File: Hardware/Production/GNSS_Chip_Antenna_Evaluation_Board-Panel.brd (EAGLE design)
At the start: 61 x 35.6 mm, 70 parts, among them J1 U.FL, J2 U.FL, J3 U.FL, J4 U.FL, J5 U.FL, J6 U.FL, Y2 PUCK, Y3 CUBE, Y4 CHIP, Y5 MOLDED, Y6 W3062A, Y7 W3011

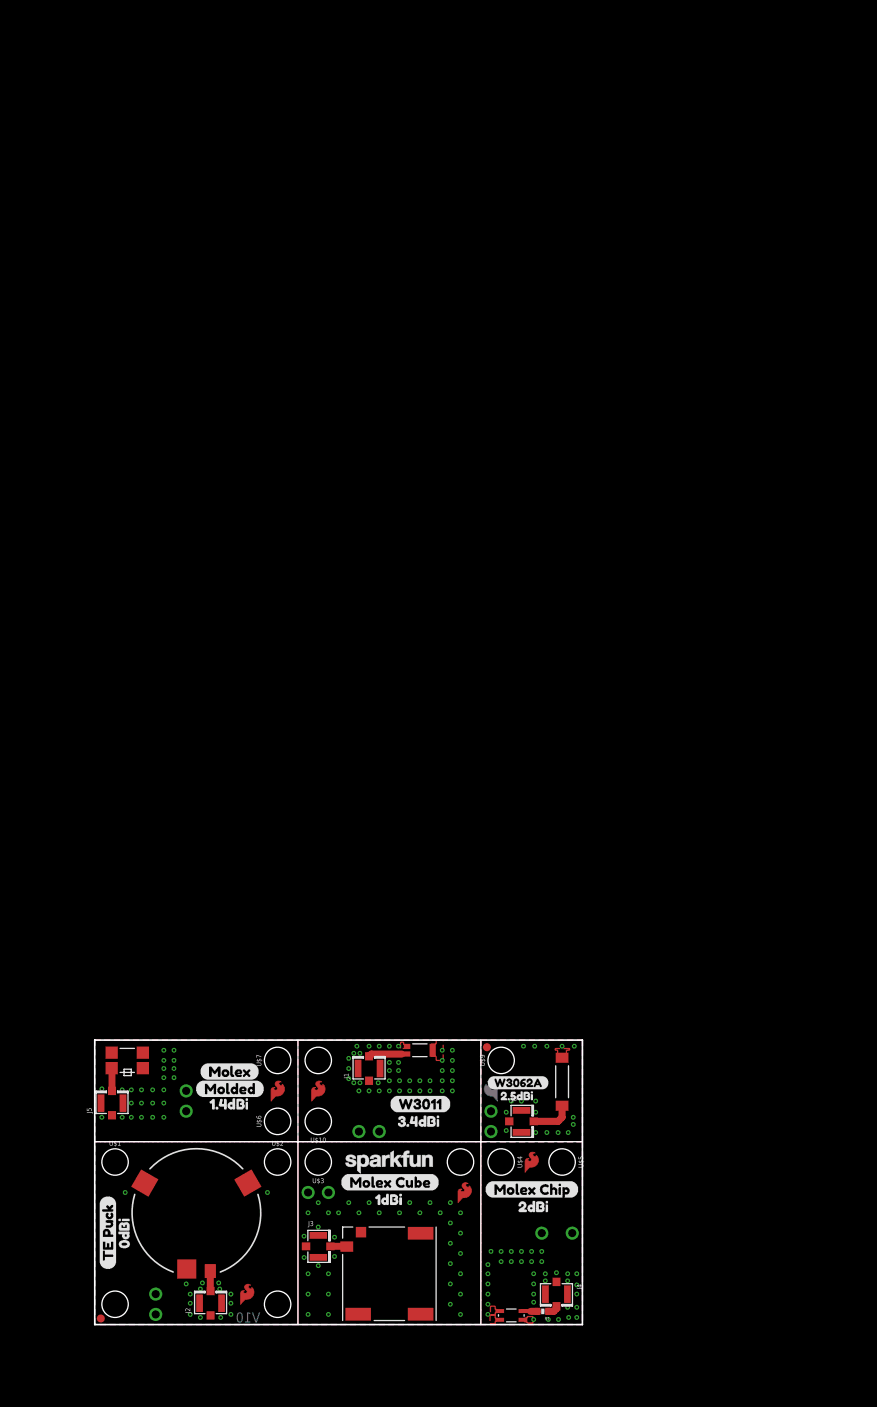
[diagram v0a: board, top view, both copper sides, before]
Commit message: Adding production panel
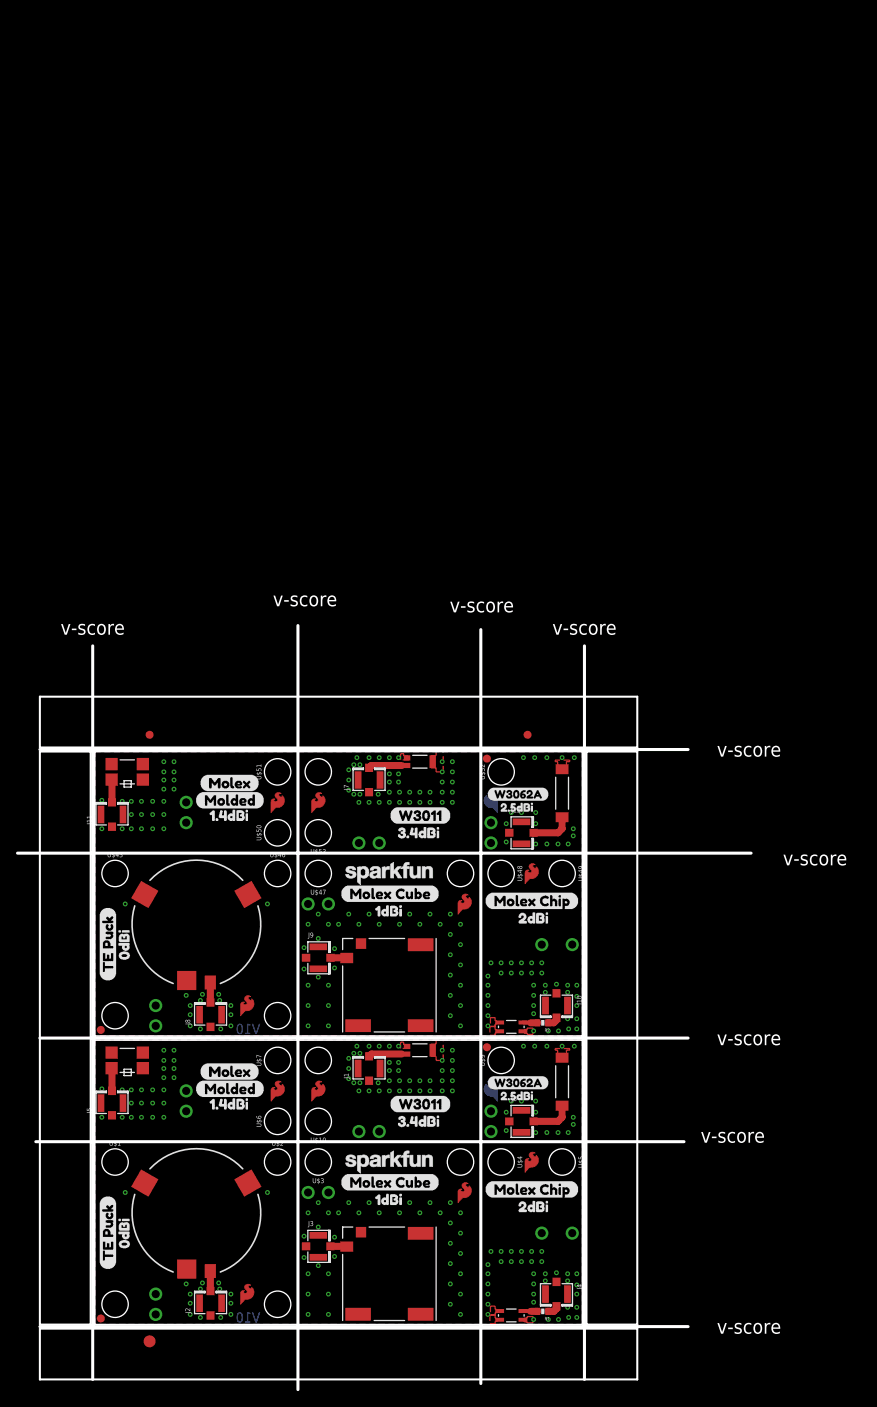
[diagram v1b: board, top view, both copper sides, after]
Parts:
- removed FRAME1: FRAME-LETTER, SparkFun-Aesthetics:CREATIVE_COMMONS
- added E$1, E$2: (no value), SparkFun-Aesthetics:FIDUCIAL-1X2
- added E$3: (no value), SparkFun-Retired:FIDUCIAL-1.5X3
- added J10, J11, J12, J7, J8, J9: U.FL, SparkFun-Connectors:U.FL
- added JP10, JP7: FIDUCIAL1X2, SparkFun:FIDUCIAL-1X2
- added JP11, JP12, JP3, JP4: STAND-OFF, SparkFun:STAND-OFF
- added LOGO10, LOGO11, LOGO12, LOGO7, LOGO8, LOGO9: SFE_LOGO_FLAME.1EXP, SparkFun-Aesthetics:SFE_LOGO_FLAME_COPPER_EXPOSED_.1
- added R2: 0, Testing:0402-RES
- added U$43, U$46, U$47, U$48, U$49, U$50, U$51, U$52, U$53: (no value), SparkFun-Hardware:STAND-OFF
- added U$54, U$75: (no value), buzzard_labels (13):3#4DBI2
- added U$55, U$74: (no value), buzzard_labels (13):W30111
- added U$56, U$83: (no value), buzzard_labels (14):0DBI0
- added U$57, U$73: (no value), buzzard_labels (14):1#4DBI3
- added U$58, U$80: (no value), buzzard_labels (14):1DBI1
- added U$59, U$79: (no value), buzzard_labels (14):2DBI2
- added U$60, U$78: (no value), buzzard_labels (14):MOLEX_CHIP7
- added U$61, U$81: (no value), buzzard_labels (14):MOLEX_CUBE6
- added U$62, U$82: (no value), buzzard_labels (14):TE_PUCK5
- added U$63, U$64, U$65, U$66, U$67, U$68: (no value), buzzard_labels (60):ANCHOR0
- added U$69, U$72: (no value), buzzard_labels (60):MOLDED2
- added U$70, U$71: (no value), buzzard_labels (60):MOLEX1
- added U$76: (no value), buzzard_labels (14):W3062A9
- added U$77: (no value), buzzard_labels (14):2#5DBI4
- added U$84: (no value), buzzard_labels (61):2#5DBI2
- added U$85: (no value), buzzard_labels (61):W3062A1
- added U$86: (no value), SparkFun-Aesthetics:SFE_LOGO_NAME_.1
- added Y1: PUCK, GNSS_Chip_Antenna_Evaluation_Board:TE_PUCK
- added Y10: MOLDED, GNSS_Chip_Antenna_Evaluation_Board:MLOEX_GNSS_MOLDED
- added Y11: W3062A, GNSS_Chip_Antenna_Evaluation_Board:W3062A
- added Y12: W3011, GNSS_Chip_Antenna_Evaluation_Board:W3011
- added Y8: CUBE, GNSS_Chip_Antenna_Evaluation_Board:MOLEX_GNSS_CUBE
- added Y9: CHIP, GNSS_Chip_Antenna_Evaluation_Board:MOLEX_GNSS_CHIP
- U$17: value (none) -> OSHW-LOGOS; device SparkFun-Aesthetics:ORDERING_INSTRUCTIONS -> SparkFun-Aesthetics:OSHW-LOGO-S
- moved U$17 47.0 mm to (19.1, 39.9), flipped to the bottom
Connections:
- new net FEED10: J10.FEED, R2.1
- new net FEED11: J11.FEED, Y10.FEED
- new net FEED12: J12.FEED, Y11.FEED
- new net FEED7: J7.FEED, Y12.1
- new net FEED8: J8.FEED, Y1.S
- new net FEED9: J9.FEED, Y8.FEED
- new net GND1: J10.1, J10.2, J11.1, J11.2, J12.1, J12.2, J7.1, J7.2, J8.1, J8.2, J9.1, J9.2, Y1.1, Y1.2, Y1.3, Y11.GND, Y12.2, Y12.3, Y8.GND, Y9.1, Y9.2, Y9.3
- new net N$2: R2.2, Y9.FEED
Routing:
- net FEED12: track 0.00 -> 5.21 mm
- net FEED7: track 0.00 -> 5.12 mm
- net FEED11: track 0.00 -> 2.92 mm
- net FEED8: track 0.00 -> 2.51 mm
- net FEED9: track 0.00 -> 2.09 mm
- net N$2: track 0.00 -> 1.86 mm
- net FEED10: track 0.00 -> 1.50 mm
- added copper zone on layer 1, net GND1
- added copper zone on layer 16, net GND1
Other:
- board size 61 x 35.6 mm -> 91.7 x 95.5 mm
- board text added: "v-score"
- board text removed: "0.8mm Board Thickness"
- board text removed: "D:/SmartProjects/Snc/a4_bn_logo2.bmp"

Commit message: Corrected the polygon FP issue on the U.FL.
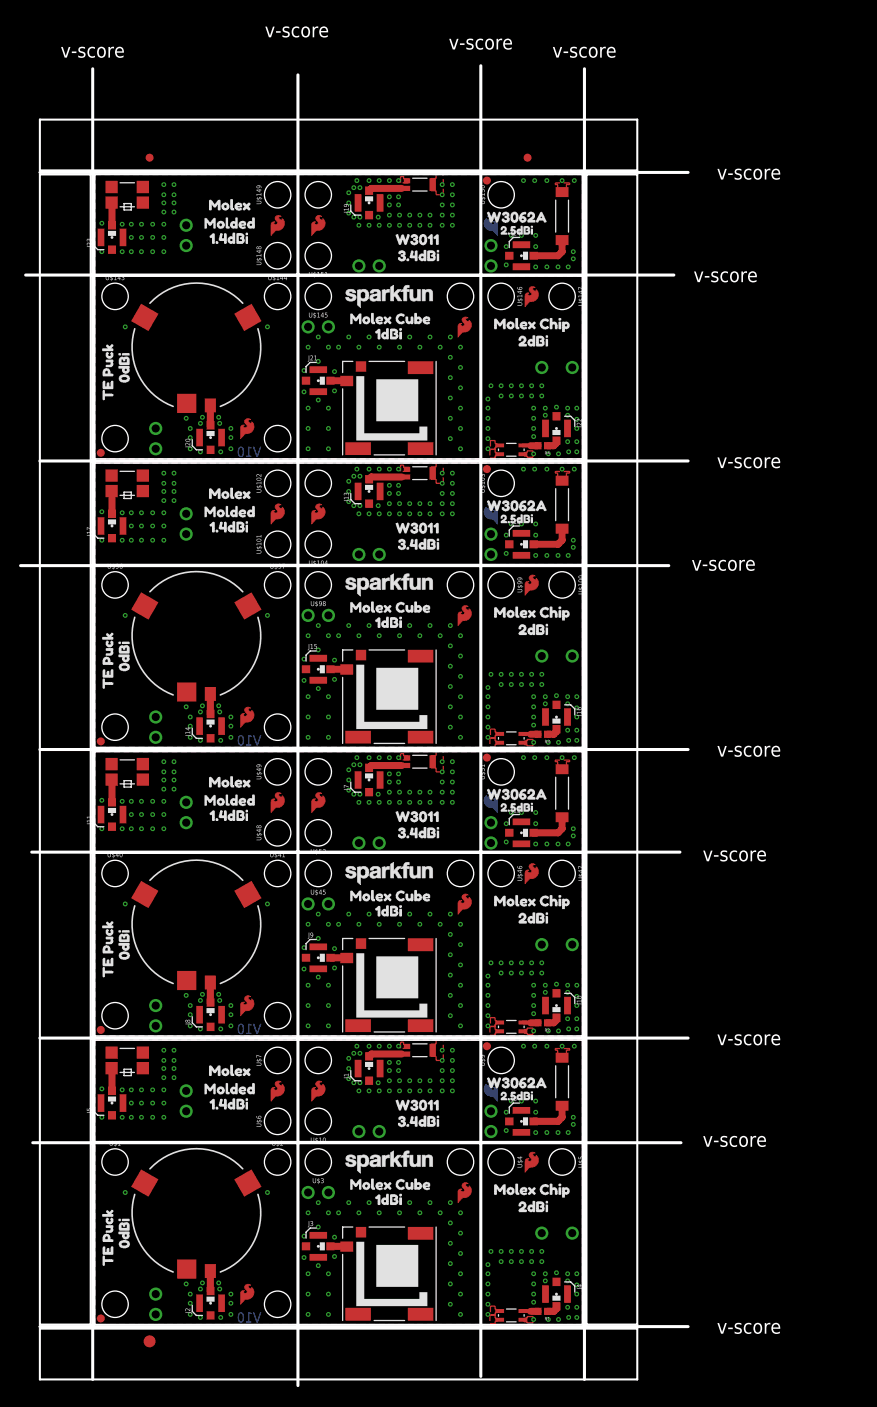
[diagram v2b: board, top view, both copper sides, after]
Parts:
- added J13, J14, J15, J16, J17, J18, J19, J20, J21, J22, J23, J24: U.FL, SparkFun-Connectors:U.FL
- added JP13, JP14, JP17, JP18, JP19, JP20, JP23, JP24: STAND-OFF, SparkFun:STAND-OFF
- added JP15, JP16, JP21, JP22: FIDUCIAL1X2, SparkFun:FIDUCIAL-1X2
- added LOGO13, LOGO14, LOGO15, LOGO16, LOGO17, LOGO18, LOGO19, LOGO20, LOGO21, LOGO22, LOGO23, LOGO24: SFE_LOGO_FLAME.1EXP, SparkFun-Aesthetics:SFE_LOGO_FLAME_COPPER_EXPOSED_.1
- added R3, R4: 0, SparkFun-Resistors:0402
- added U$100, U$101, U$102, U$103, U$104, U$143, U$144, U$145, U$146, U$147, U$148, U$149, U$150, U$151, U$96, U$97, U$98, U$99: (no value), SparkFun-Hardware:STAND-OFF
- added U$105, U$117, U$152, U$164: (no value), buzzard_labels (13):3#4DBI2
- added U$106, U$121, U$153, U$168: (no value), buzzard_labels (14):0DBI0
- added U$107, U$116, U$154, U$163: (no value), buzzard_labels (14):1#4DBI3
- added U$108, U$120, U$155, U$167: (no value), buzzard_labels (14):1DBI1
- added U$109, U$119, U$156, U$166: (no value), buzzard_labels (14):2DBI2
- added U$110, U$111, U$112, U$113, U$114, U$115, U$157, U$158, U$159, U$160, U$161, U$162: (no value), buzzard_labels (60):ANCHOR0
- added U$118, U$165: (no value), buzzard_labels (14):2#5DBI4
- added U$122, U$169: (no value), buzzard_labels (61):2#5DBI2
- added U$123, U$170: (no value), SparkFun-Aesthetics:SFE_LOGO_NAME_.1
- added U$124, U$171: (no value), buzzard_labels (1):ANTENNA10
- added U$125, U$172: (no value), buzzard_labels (1):EVALUATION_BOARD15
- added U$126, U$173: (no value), buzzard_labels (1):GNSS_CHIP13
- added U$127, U$138, U$174, U$185, U$91: (no value), buzzard_labels (1):MOLEX_CUBE6
- added U$128, U$131, U$175, U$178: (no value), buzzard_labels (1):TE_PUCK7
- added U$129, U$140, U$176, U$187, U$93: (no value), buzzard_labels (1):W3062A3
- added U$130, U$139, U$177, U$186, U$92: (no value), buzzard_labels (1):W30112
- added U$132, U$133, U$179, U$180: (no value), buzzard_labels (1):MOLEX_CHIP5
- added U$134, U$136, U$181, U$183, U$87, U$89: (no value), buzzard_labels (1):MOLEX0
- added U$135, U$137, U$182, U$184, U$88, U$90: (no value), buzzard_labels (1):MOLDED1
- added U$141, U$188, U$94: (no value), SparkFun-Aesthetics:SFE_LOGO_NAME_FLAME_.1
- added U$142, U$95: OSHW-LOGOS, SparkFun-Aesthetics:OSHW-LOGO-S
- added Y13, Y19: PUCK, SparkFun-GPS:TE_PUCK
- added Y14, Y20: CUBE, SparkFun-GPS:MOLEX_GNSS_CUBE
- added Y15, Y21: CHIP, SparkFun-GPS:MOLEX_GNSS_CHIP
- added Y16, Y22: MOLDED, SparkFun-GPS:MLOEX_GNSS_MOLDED
- added Y17, Y23: W3062A, SparkFun-GPS:W3062A
- added Y18, Y24: W3011, SparkFun-GPS:W3011
- R1, R2: device Testing:0402-RES -> SparkFun-Resistors:0402
- U$13: device buzzard_labels (13):W30111 -> buzzard_labels (1):TE_PUCK7
- U$19: device buzzard_labels (14):MOLEX_CHIP7 -> buzzard_labels (1):MOLEX_CHIP5
- U$20: device buzzard_labels (14):MOLEX_CUBE6 -> buzzard_labels (1):MOLEX_CHIP5
- U$21: device buzzard_labels (60):MOLEX1 -> buzzard_labels (1):MOLEX0
- U$22: device buzzard_labels (14):TE_PUCK5 -> buzzard_labels (1):MOLEX0
- U$29: device buzzard_labels (60):MOLDED2 -> buzzard_labels (1):MOLDED1
- U$30: device buzzard_labels (60):MOLEX1 -> buzzard_labels (1):MOLDED1
- U$31: device buzzard_labels (60):MOLDED2 -> buzzard_labels (1):MOLEX_CUBE6
- U$33: device buzzard_labels (13):W30111 -> buzzard_labels (1):W30112
- U$35: device buzzard_labels (14):W3062A9 -> buzzard_labels (1):W3062A3
- U$37: device buzzard_labels (14):MOLEX_CHIP7 -> SparkFun-Aesthetics:SFE_LOGO_NAME_FLAME_.1
- U$40: device buzzard_labels (14):MOLEX_CUBE6 -> SparkFun-Hardware:STAND-OFF
- U$41: device buzzard_labels (14):TE_PUCK5 -> SparkFun-Hardware:STAND-OFF
- U$43: device SparkFun-Hardware:STAND-OFF -> buzzard_labels (1):ANTENNA10
- U$45: device buzzard_labels (61):W3062A1 -> SparkFun-Hardware:STAND-OFF
- U$50: device SparkFun-Hardware:STAND-OFF -> buzzard_labels (1):EVALUATION_BOARD15
- U$52: device SparkFun-Hardware:STAND-OFF -> buzzard_labels (1):GNSS_CHIP13
- U$55, U$74: device buzzard_labels (13):W30111 -> buzzard_labels (14):0DBI0
- U$56: device buzzard_labels (14):0DBI0 -> buzzard_labels (1):MOLEX_CUBE6
- U$57: device buzzard_labels (14):1#4DBI3 -> buzzard_labels (1):TE_PUCK7
- U$58: device buzzard_labels (14):1DBI1 -> buzzard_labels (1):W3062A3
- U$59: device buzzard_labels (14):2DBI2 -> buzzard_labels (1):W30112
- U$60: device buzzard_labels (14):MOLEX_CHIP7 -> buzzard_labels (14):1#4DBI3
- U$61: device buzzard_labels (14):MOLEX_CUBE6 -> buzzard_labels (14):1DBI1
- U$62: device buzzard_labels (14):TE_PUCK5 -> buzzard_labels (14):2DBI2
- U$69: device buzzard_labels (60):MOLDED2 -> buzzard_labels (14):1#4DBI3
- U$70: device buzzard_labels (60):MOLEX1 -> buzzard_labels (13):3#4DBI2
- U$71: device buzzard_labels (60):MOLEX1 -> buzzard_labels (14):2#5DBI4
- U$72: device buzzard_labels (60):MOLDED2 -> buzzard_labels (14):2DBI2
- U$73: device buzzard_labels (14):1#4DBI3 -> buzzard_labels (14):1DBI1
- U$75: device buzzard_labels (13):3#4DBI2 -> buzzard_labels (61):2#5DBI2
- U$76: device buzzard_labels (14):W3062A9 -> SparkFun-Aesthetics:SFE_LOGO_NAME_.1
- U$77: device buzzard_labels (14):2#5DBI4 -> buzzard_labels (1):ANTENNA10
- U$78: device buzzard_labels (14):MOLEX_CHIP7 -> buzzard_labels (1):EVALUATION_BOARD15
- U$79: device buzzard_labels (14):2DBI2 -> buzzard_labels (1):GNSS_CHIP13
- U$80: device buzzard_labels (14):1DBI1 -> buzzard_labels (1):MOLEX_CUBE6
- U$81: device buzzard_labels (14):MOLEX_CUBE6 -> buzzard_labels (1):TE_PUCK7
- U$82: device buzzard_labels (14):TE_PUCK5 -> buzzard_labels (1):W3062A3
- U$83: device buzzard_labels (14):0DBI0 -> buzzard_labels (1):W30112
- U$84: device buzzard_labels (61):2#5DBI2 -> buzzard_labels (1):TE_PUCK7
- U$85: device buzzard_labels (61):W3062A1 -> buzzard_labels (1):MOLEX_CHIP5
- U$86: device SparkFun-Aesthetics:SFE_LOGO_NAME_.1 -> buzzard_labels (1):MOLEX_CHIP5
- Y1, Y2: device GNSS_Chip_Antenna_Evaluation_Board:TE_PUCK -> SparkFun-GPS:TE_PUCK
- Y10, Y5: device GNSS_Chip_Antenna_Evaluation_Board:MLOEX_GNSS_MOLDED -> SparkFun-GPS:MLOEX_GNSS_MOLDED
- Y11, Y6: device GNSS_Chip_Antenna_Evaluation_Board:W3062A -> SparkFun-GPS:W3062A
- Y12, Y7: device GNSS_Chip_Antenna_Evaluation_Board:W3011 -> SparkFun-GPS:W3011
- Y3, Y8: device GNSS_Chip_Antenna_Evaluation_Board:MOLEX_GNSS_CUBE -> SparkFun-GPS:MOLEX_GNSS_CUBE
- Y4, Y9: device GNSS_Chip_Antenna_Evaluation_Board:MOLEX_GNSS_CHIP -> SparkFun-GPS:MOLEX_GNSS_CHIP
- moved E$1 72.1 mm to (6.86, 145.9)
- moved E$2 72.1 mm to (54.1, 145.9)
- moved U$40 59.6 mm to (2.54, 56.4), flipped to the top
- moved U$52 59.3 mm to (18.2, 19.6), flipped to the bottom, turned to 0 degrees
- moved U$57 58.6 mm to (1.65, 6.22), turned to 90 degrees
- moved U$62 50.8 mm to (51.8, 50.8), turned to 0 degrees
- moved U$37 48.3 mm to (12.8, 9.65)
- moved U$50 46.9 mm to (21.3, 14.6), flipped to the bottom, turned to 0 degrees
- moved U$41 44.0 mm to (22.9, 56.4), flipped to the top
- moved U$77 42.2 mm to (17.5, 53.1), turned to 0 degrees
- moved U$43 42.1 mm to (17.5, 17.0), flipped to the bottom
- moved U$81 41.9 mm to (1.65, 42.3), flipped to the top, turned to 90 degrees
- moved U$79 40.0 mm to (18.2, 55.6)
- moved U$72 39.5 mm to (57.9, 50.8)
- moved U$78 39.3 mm to (21.3, 50.7)
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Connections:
- new net FEED13: J13.FEED, Y18.1
- new net FEED14: J14.FEED, Y13.S
- new net FEED15: J15.FEED, Y14.FEED
- new net FEED16: J16.FEED, R3.1
- new net FEED17: J17.FEED, Y16.FEED
- new net FEED18: J18.FEED, Y17.FEED
- new net FEED19: J19.FEED, Y24.1
- new net FEED20: J20.FEED, Y19.S
- new net FEED21: J21.FEED, Y20.FEED
- new net FEED22: J22.FEED, R4.1
- new net FEED23: J23.FEED, Y22.FEED
- new net FEED24: J24.FEED, Y23.FEED
- new net GND2: J13.1, J13.2, J14.1, J14.2, J15.1, J15.2, J16.1, J16.2, J17.1, J17.2, J18.1, J18.2, Y13.1, Y13.2, Y13.3, Y14.GND, Y15.1, Y15.2, Y15.3, Y17.GND, Y18.2, Y18.3
- new net GND3: J19.1, J19.2, J20.1, J20.2, J21.1, J21.2, J22.1, J22.2, J23.1, J23.2, J24.1, J24.2, Y19.1, Y19.2, Y19.3, Y20.GND, Y21.1, Y21.2, Y21.3, Y23.GND, Y24.2, Y24.3
- new net N$25: R3.2, Y15.FEED
- new net N$37: R4.2, Y21.FEED
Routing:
- net FEED18: track 0.00 -> 5.21 mm
- net FEED24: track 0.00 -> 5.21 mm
- net FEED19: track 0.00 -> 5.12 mm
- net FEED13: track 0.00 -> 5.12 mm
- net FEED17: track 0.00 -> 2.86 mm
- net FEED23: track 0.00 -> 2.86 mm
- net FEED20: track 0.00 -> 2.51 mm
- net FEED14: track 0.00 -> 2.51 mm
- net FEED21: track 0.00 -> 2.05 mm
- net FEED15: track 0.00 -> 2.05 mm
- net N$37: track 0.00 -> 1.93 mm
- net N$25: track 0.00 -> 1.93 mm
- net FEED22: track 0.00 -> 1.57 mm
- net FEED16: track 0.00 -> 1.57 mm
- added copper zone on layer 1, net GND2
- added copper zone on layer 16, net GND2
- added copper zone on layer 1, net GND3
- added copper zone on layer 16, net GND3
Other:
- board size 91.7 x 95.5 mm -> 83.4 x 165 mm
